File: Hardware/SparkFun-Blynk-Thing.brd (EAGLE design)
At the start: 50 x 41.9 mm, 103 parts, among them IC1 LMV358, Q1 2.5A/30V, Q2 MMBT2222A, Q3 MMBT2222A, U1 MCP73831, U2 ESP8266, U3 AP2112K-3.3V, U4 FT231XS-U, U5 W25Q32FVSS, U6 SI7021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

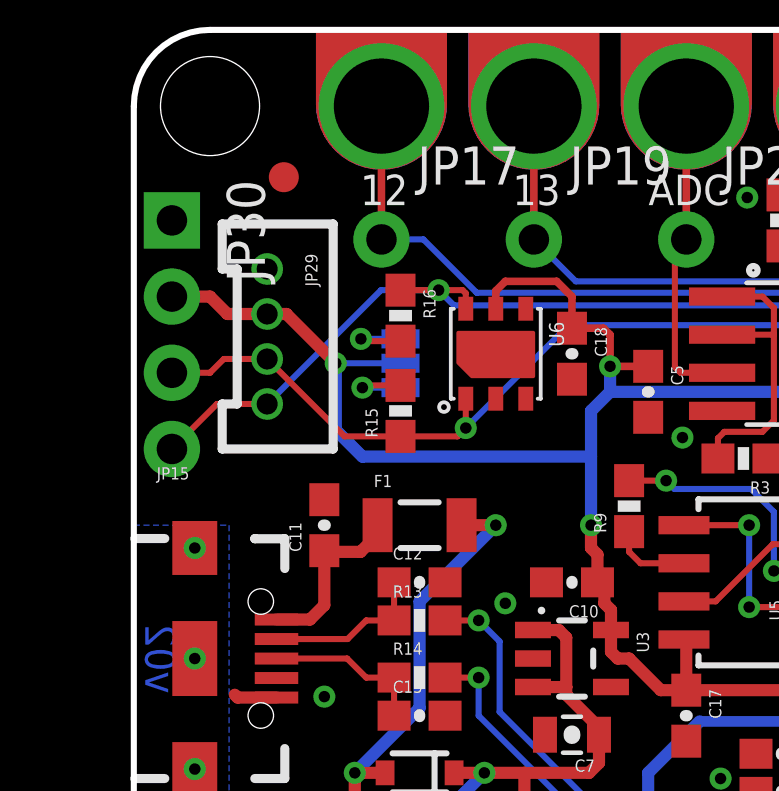
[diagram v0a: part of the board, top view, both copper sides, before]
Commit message: Swapping JST connectors on I2C footprint.
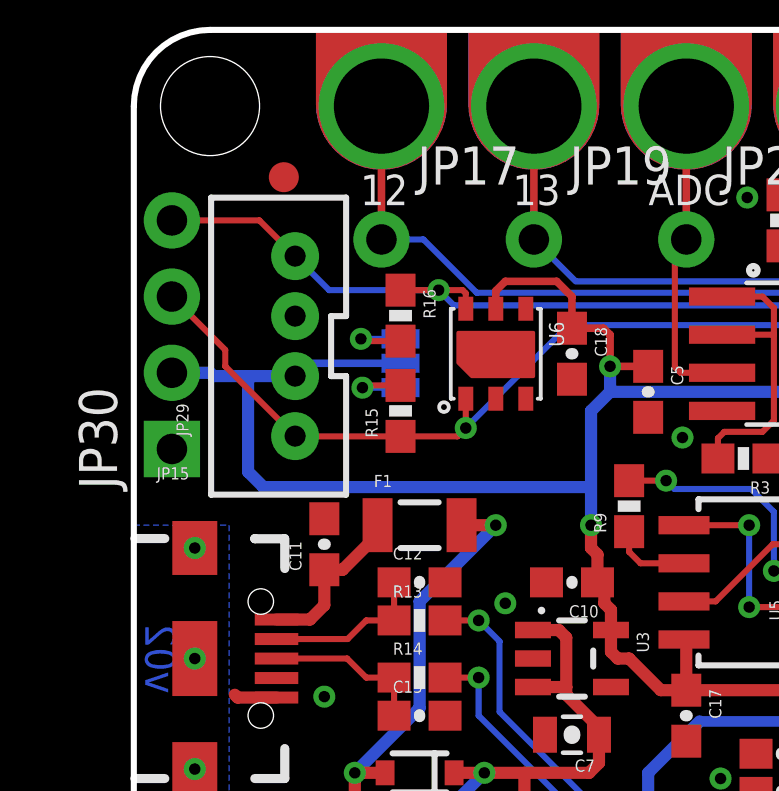
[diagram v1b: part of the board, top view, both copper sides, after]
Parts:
- JP29: device SparkFun-Connectors:1X04-1.5MM_JST -> SparkFun-Connectors:JST-4-PTH-VERT
- moved JP30 7.62 mm to (1.27, 27.9), turned to 90 degrees
- moved JP29 2.60 mm to (4.83, 31.4), turned to 90 degrees
- moved C11 0.63 mm to (6.35, 24.8)
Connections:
- net 2/SDA: now also JP29.1; no longer JP29.3
- net GND: now also JP29.3; no longer JP29.1
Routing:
- net VCC: track 164.2 -> 167.2 mm, vias 14 -> 13
- net 14/SCL: track 41.9 -> 40.7 mm
- net 2/SDA: track 36.1 -> 37.1 mm

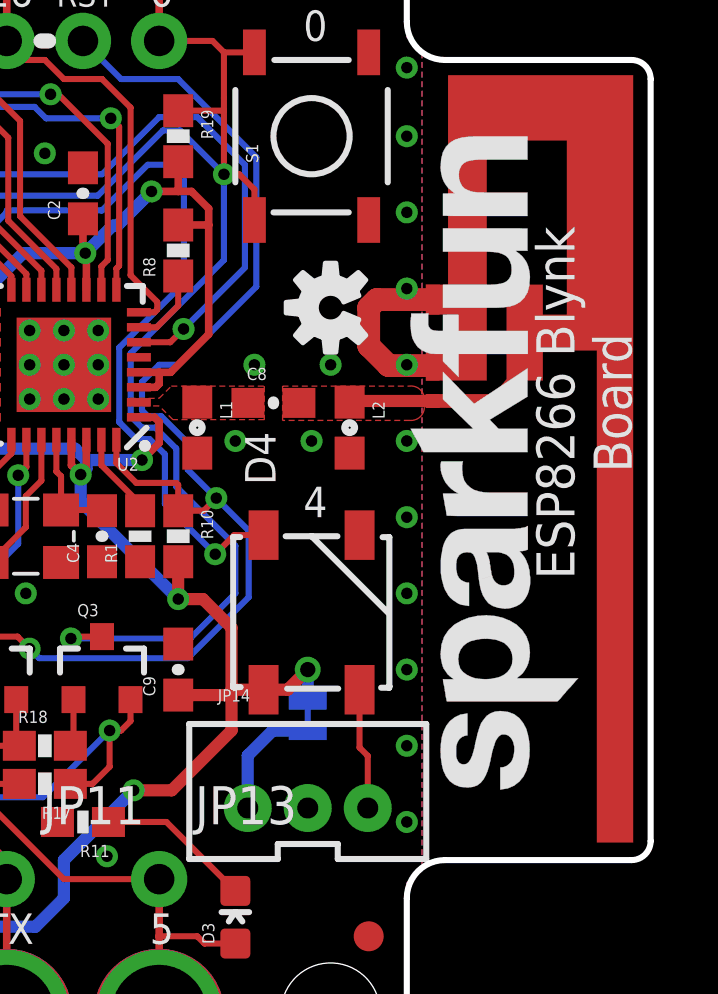
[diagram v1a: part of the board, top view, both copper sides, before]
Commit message: Silkscreen fixes
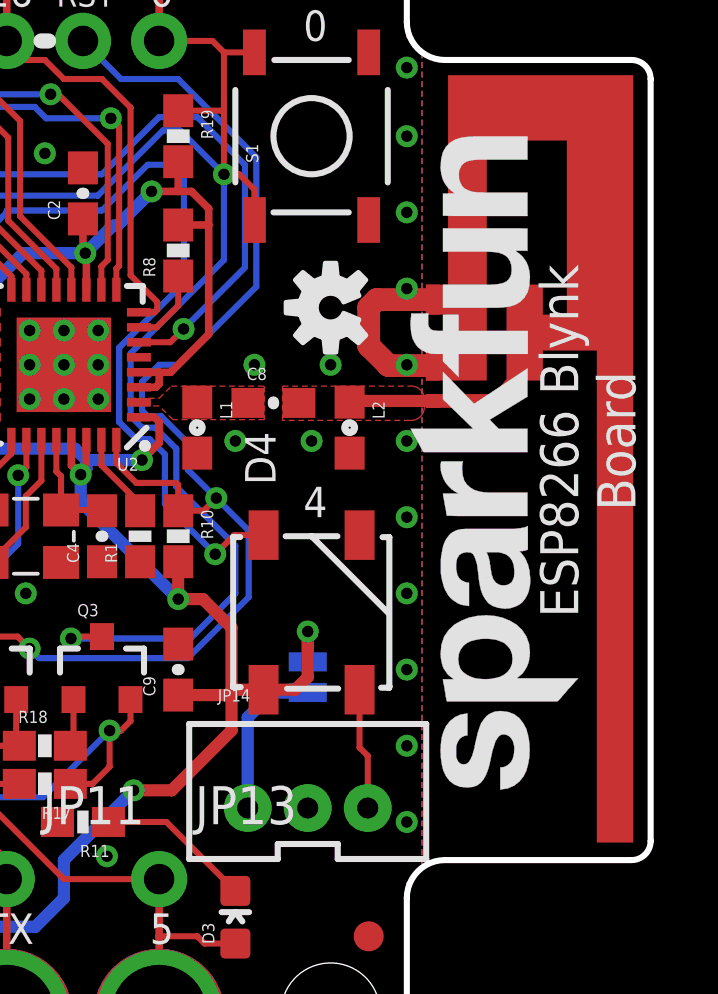
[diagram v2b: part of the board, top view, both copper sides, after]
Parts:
- moved SJ3 1.27 mm to (38.6, 13.7)
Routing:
- net VCC: track 167.2 -> 168.6 mm
- net N$19: track 4.09 -> 5.36 mm
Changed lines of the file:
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@@
 PU</text>
 <text x="38.862" y="34.925" size="1.016" layer="21" ratio="15" rot="R180" align="top-center">0</text>
-<text x="37.3253" y="12.446" size="0.8128" layer="22" font="vector" ratio="15" rot="MR0" align="center-left">WS2812
+<text x="37.3253" y="13.716" size="0.8128" layer="22" font="vector" ratio="15" rot="MR0" align="center-left">WS2812
 VCC</text>
 <text x="2.54" y="8.255" size="1.016" layer="21" font="vector" ratio="15" rot="R180" align="bottom-center">CHG</text>
@@
 <text x="31.0261" y="36.8808" size="0.8128" layer="22" ratio="15" rot="MR180" align="bottom-center">RST</text>
 <text x="33.5661" y="37.084" size="1.016" layer="22" ratio="15" rot="MR180" align="bottom-center">0</text>
-<text x="46.228" y="22.86" size="1.27" layer="21" ratio="15" rot="R90" align="top-center">ESP8266 Blynk
+<text x="46.355" y="21.59" size="1.27" layer="21" ratio="15" rot="R90" align="top-center">ESP8266 Blynk
 Board</text>
+<text x="6.35" y="32.385" size="0.8128" layer="22" font="vector" ratio="15" rot="MR90" align="bottom-center">GND</text>
+<wire x1="3.556" y1="35.56" x2="5.334" y2="34.417" width="0.2032" layer="22"/>
+<wire x1="3.683" y1="30.48" x2="5.334" y2="30.353" width="0.2032" layer="22"/>
+<text x="6.35" y="28.575" size="0.8128" layer="22" font="vector" ratio="15" rot="MR90" align="bottom-center">SDA</text>
 </plain>
 <attributes>
@@
 <element name="JP3" library="SparkFun-Connectors" package="1X01_NO_SILK" value="" x="8.255" y="6.985"/>
 <element name="SJ4" library="SparkFun-Passives" package="PAD-JUMPER-3-3OF3_NC_BY_TRACE_YES_SILK_FULL_BOX" value="" x="8.89" y="30.7975" rot="MR270"/>
-<element name="SJ3" library="SparkFun-Passives" package="PAD-JUMPER-2-NC_BY_TRACE_YES_SILK" value="WS2812-VCC" x="38.608" y="12.446" rot="MR90"/>
+<element name="SJ3" library="SparkFun-Passives" package="PAD-JUMPER-2-NC_BY_TRACE_YES_SILK" value="WS2812-VCC" x="38.608" y="13.716" rot="MR90"/>
 <element name="JP30" library="SparkFun-Connectors" package="1X04_NO_SILK" value="" x="1.27" y="27.94" rot="R90"/>
 <element name="C19" library="SparkFun-Capacitors" package="0603-CAP" value="4.7uF" x="15.875" y="6.35" rot="R270">
@@
 <wire x1="29.5275" y1="5.3975" x2="13.335" y2="5.3975" width="0.4064" layer="16"/>
 <wire x1="13.335" y1="5.3975" x2="6.6675" y2="5.3975" width="0.4064" layer="16"/>
-<wire x1="38.608" y1="12.954" x2="38.608" y2="13.97" width="0.4064" layer="16"/>
-<via x="38.608" y="13.97" extent="1-16" drill="0.508"/>
-<wire x1="38.608" y1="13.97" x2="37.936" y2="13.298" width="0.4064" layer="1"/>
-<wire x1="37.936" y1="13.298" x2="37.135" y2="13.298" width="0.4064" layer="1"/>
 <wire x1="37.135" y1="13.298" x2="36.068" y2="13.298" width="0.4064" layer="1"/>
 <wire x1="34.29" y1="13.12" x2="36.068" y2="13.12" width="0.4064" layer="1"/>
@@
 <wire x1="5.376" y1="30.369" x2="5.8045" y2="30.7975" width="0.254" layer="16"/>
 <wire x1="5.8045" y1="30.7975" x2="8.89" y2="30.7975" width="0.254" layer="16"/>
+<wire x1="37.135" y1="13.298" x2="38.19" y2="13.298" width="0.4064" layer="1"/>
+<wire x1="38.19" y1="13.298" x2="38.608" y2="13.716" width="0.4064" layer="1"/>
+<wire x1="38.608" y1="13.716" x2="38.608" y2="15.24" width="0.4064" layer="1"/>
+<via x="38.608" y="15.24" extent="1-16" drill="0.381"/>
+<wire x1="38.608" y1="15.24" x2="38.608" y2="14.224" width="0.4064" layer="16"/>
 </signal>
 <signal name="GND">
@@
 <contactref element="JP14" pad="1"/>
 <contactref element="SJ3" pad="1"/>
-<wire x1="36.608" y1="9.356" x2="36.608" y2="11.1064" width="0.4064" layer="16"/>
-<wire x1="38.608" y1="11.938" x2="37.4396" y2="11.938" width="0.4064" layer="16"/>
-<wire x1="37.4396" y1="11.938" x2="36.608" y2="11.1064" width="0.4064" layer="16"/>
+<wire x1="36.608" y1="9.356" x2="36.608" y2="12.3764" width="0.4064" layer="16"/>
+<wire x1="38.608" y1="13.208" x2="37.4396" y2="13.208" width="0.4064" layer="16"/>
+<wire x1="37.4396" y1="13.208" x2="36.608" y2="12.3764" width="0.4064" layer="16"/>
 </signal>
 </signals>

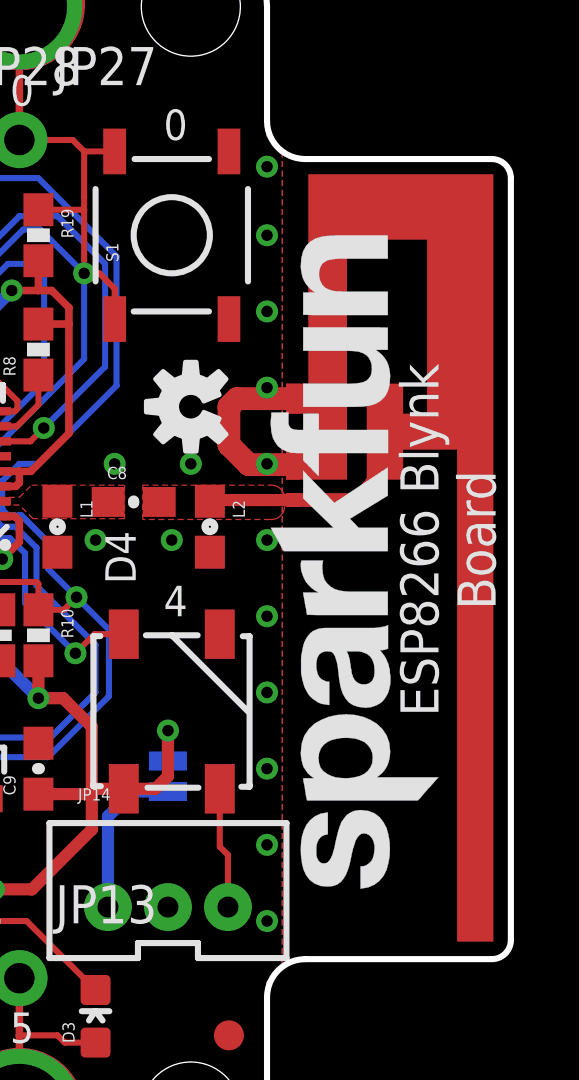
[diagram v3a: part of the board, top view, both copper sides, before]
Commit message: Updating board name on silkscreen.
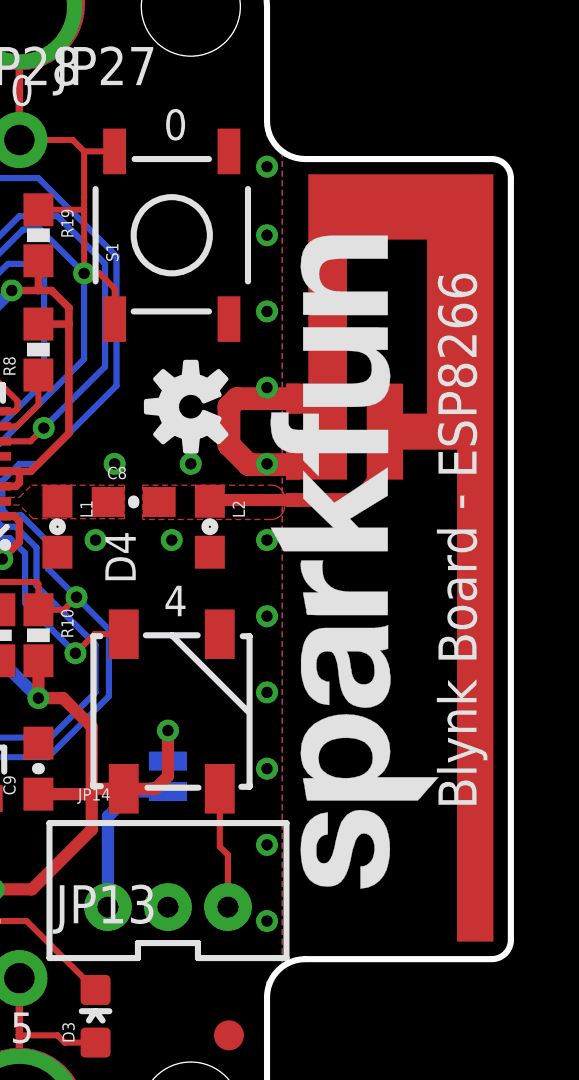
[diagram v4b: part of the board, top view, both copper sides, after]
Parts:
- added LOGO3: SFE_LOGO_NAME.3_INCH, SparkFun-Aesthetics:SFE_LOGO_NAME_.3
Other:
- board text added: "Blynk Board - ESP8266"
- board text removed: "ESP8266 Blynk Board"
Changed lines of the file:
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@@
 <text x="31.0261" y="36.8808" size="0.8128" layer="22" ratio="15" rot="MR180" align="bottom-center">RST</text>
 <text x="33.5661" y="37.084" size="1.016" layer="22" ratio="15" rot="MR180" align="bottom-center">0</text>
-<text x="46.355" y="21.59" size="1.27" layer="21" ratio="15" rot="R90" align="top-center">ESP8266 Blynk
-Board</text>
+<text x="47.625" y="21.59" size="1.27" layer="21" ratio="15" rot="R90" align="top-center">Blynk Board - ESP8266</text>
 <text x="6.35" y="32.385" size="0.8128" layer="22" font="vector" ratio="15" rot="MR90" align="bottom-center">GND</text>
 <wire x1="3.556" y1="35.56" x2="5.334" y2="34.417" width="0.2032" layer="22"/>
 <wire x1="3.683" y1="30.48" x2="5.334" y2="30.353" width="0.2032" layer="22"/>
 <text x="6.35" y="28.575" size="0.8128" layer="22" font="vector" ratio="15" rot="MR90" align="bottom-center">SDA</text>
+<text x="20.32" y="17.78" size="1.778" layer="22" ratio="15" rot="MR0" align="top-center">Blynk Board - ESP8266</text>
 </plain>
 <attributes>
@@
 <attribute name="PROD_ID" value="TBD" x="4.826" y="31.369" size="1.778" layer="27" rot="R90" display="off"/>
 </element>
+<element name="LOGO3" library="SparkFun-Aesthetics" package="SFE_LOGO_NAME_.3" value="SFE_LOGO_NAME.3_INCH" x="39.37" y="17.78" rot="MR0"/>
 </elements>
 <signals>
